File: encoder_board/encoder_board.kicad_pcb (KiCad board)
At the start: 2 copper layers, 40 x 10 mm, 8 parts, among them J1 Conn_01x06, U1 AS5048A

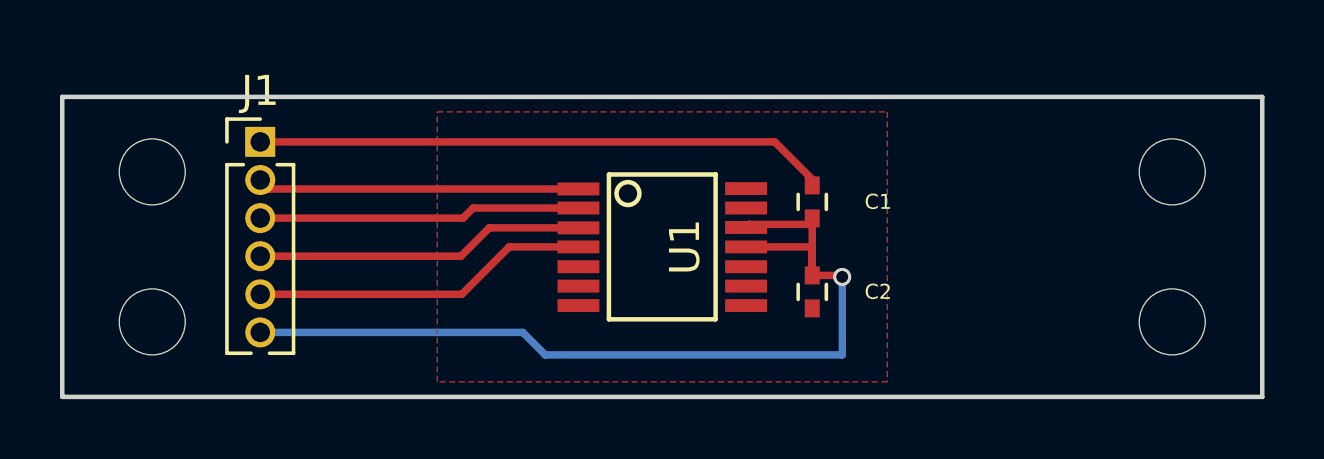
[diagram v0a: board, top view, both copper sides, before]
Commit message: move ground plane to back
 - rexport encoder step
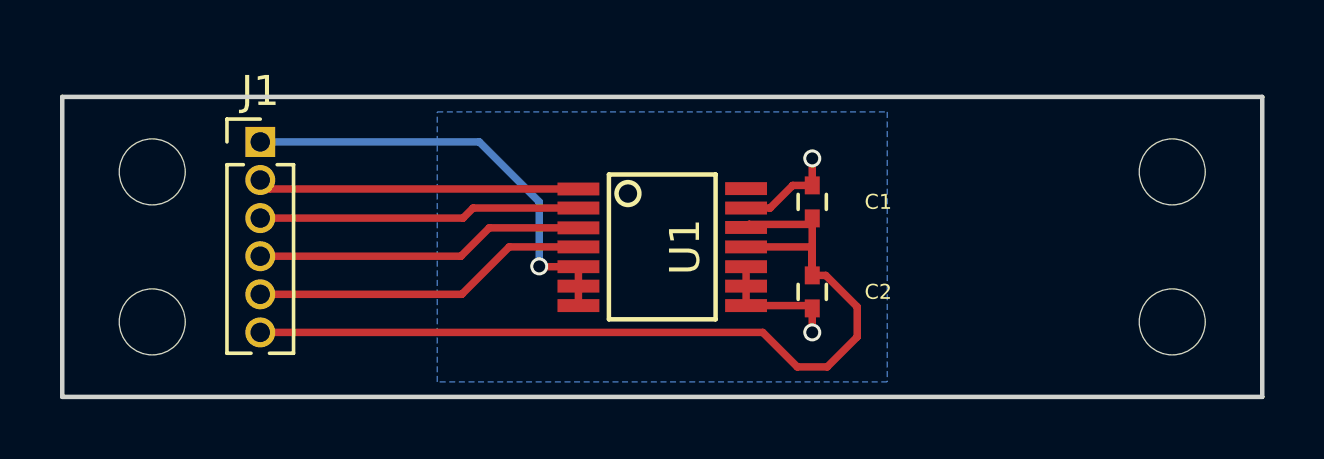
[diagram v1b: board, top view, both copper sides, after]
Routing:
- net GND: track 18.9 -> 22.6 mm, vias 0 -> 3
- net +3V3: track 30.9 -> 31.2 mm, vias 1 -> 0
- added copper zone on B.Cu, net GND
- removed copper zone on F.Cu, net GND
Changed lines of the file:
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@@
     (thickness 1.6)
     (drawings 6)
-    (tracks 27)
+    (tracks 44)
     (zones 0)
     (modules 8)
@@
   (gr_line (start 140 100) (end 140 110) (angle 90) (layer Edge.Cuts) (width 0.15))
   (gr_line (start 100 100) (end 140 100) (angle 90) (layer Edge.Cuts) (width 0.15))
-  (segment (start 106.6 101.5) (end 123.75 101.5) (width 0.25) (layer F.Cu) (net 1) (status 10))
-  (segment (start 123.75 101.5) (end 125 102.75) (width 0.25) (layer F.Cu) (net 1))
-  (segment (start 125 105.95) (end 125.95 105.95) (width 0.25) (layer F.Cu) (net 3))
-  (segment (start 115.35 107.85) (end 106.6 107.85) (width 0.25) (layer B.Cu) (net 3))
-  (segment (start 116.1 108.6) (end 115.35 107.85) (width 0.25) (layer B.Cu) (net 3))
-  (segment (start 126 108.6) (end 116.1 108.6) (width 0.25) (layer B.Cu) (net 3))
-  (segment (start 126 106) (end 126 108.6) (width 0.25) (layer B.Cu) (net 3))
-  (via (at 126 106) (size 0.6) (drill 0.4) (layers F.Cu B.Cu) (net 3))
-  (segment (start 125.95 105.95) (end 126 106) (width 0.25) (layer F.Cu) (net 3))
+  (segment (start 125 107.05) (end 125 107.85) (width 0.25) (layer F.Cu) (net 1) (status 400000))
+  (via (at 125 107.85) (size 0.6) (drill 0.4) (layers F.Cu B.Cu) (net 1))
+  (segment (start 122.794 106.9558) (end 124.9058 106.9558) (width 0.25) (layer F.Cu) (net 1) (status C00000))
+  (segment (start 124.9058 106.9558) (end 125 107.05) (width 0.25) (layer F.Cu) (net 1) (status C00000))
+  (segment (start 125 102.95) (end 125 102.05) (width 0.25) (layer F.Cu) (net 1) (status 400000))
+  (via (at 125 102.05) (size 0.6) (drill 0.4) (layers F.Cu B.Cu) (net 1))
+  (segment (start 122.794 103.7046) (end 123.5954 103.7046) (width 0.25) (layer F.Cu) (net 1) (status 400000))
+  (segment (start 124.35 102.95) (end 125 102.95) (width 0.25) (layer F.Cu) (net 1) (status 800000))
+  (segment (start 123.5954 103.7046) (end 124.35 102.95) (width 0.25) (layer F.Cu) (net 1))
+  (segment (start 122.794 106.3081) (end 122.794 105.6604) (width 0.25) (layer F.Cu) (net 1) (status C00000))
+  (segment (start 122.794 106.9558) (end 122.794 106.3081) (width 0.25) (layer F.Cu) (net 1) (status C00000))
+  (segment (start 117.206 106.3081) (end 117.206 105.6604) (width 0.25) (layer F.Cu) (net 1) (status C00000))
+  (segment (start 117.206 106.9558) (end 117.206 106.3081) (width 0.25) (layer F.Cu) (net 1) (status C00000))
+  (segment (start 106.6 101.5) (end 113.9 101.5) (width 0.25) (layer B.Cu) (net 1) (status 400000))
+  (segment (start 113.9 101.5) (end 115.9 103.5) (width 0.25) (layer B.Cu) (net 1))
+  (segment (start 115.9 103.5) (end 115.9 105.65) (width 0.25) (layer B.Cu) (net 1))
+  (segment (start 115.9104 105.6604) (end 117.206 105.6604) (width 0.25) (layer F.Cu) (net 1) (status 800000))
+  (via (at 115.9 105.65) (size 0.6) (drill 0.4) (layers F.Cu B.Cu) (net 1))
+  (segment (start 115.9104 105.6604) (end 115.9 105.65) (width 0.25) (layer F.Cu) (net 1))
+  (segment (start 106.6 107.85) (end 123.35 107.85) (width 0.25) (layer F.Cu) (net 3) (status 400000))
+  (segment (start 125.45 105.95) (end 125 105.95) (width 0.25) (layer F.Cu) (net 3) (status 800000))
+  (segment (start 126.5 107) (end 125.45 105.95) (width 0.25) (layer F.Cu) (net 3))
+  (segment (start 126.5 108) (end 126.5 107) (width 0.25) (layer F.Cu) (net 3))
+  (segment (start 125.5 109) (end 126.5 108) (width 0.25) (layer F.Cu) (net 3))
+  (segment (start 124.5 109) (end 125.5 109) (width 0.25) (layer F.Cu) (net 3))
+  (segment (start 123.35 107.85) (end 124.5 109) (width 0.25) (layer F.Cu) (net 3))
   (segment (start 125 105.95) (end 125 105) (width 0.25) (layer F.Cu) (net 3))
   (segment (start 125 105) (end 122.794 105) (width 0.25) (layer F.Cu) (net 3))
@@
   (segment (start 113.32 106.58) (end 114.9 105) (width 0.25) (layer F.Cu) (net 7))
   (segment (start 114.9 105) (end 117.206 105) (width 0.25) (layer F.Cu) (net 7))
-  (zone (net 1) (net_name GND) (layer F.Cu) (hatch edge 0.508)
+  (zone (net 1) (net_name GND) (layer B.Cu) (hatch edge 0.508)
     (connect_pads (clearance 0.25))
     (min_thickness 0.25)

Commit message: apply cosine's suggestions about gnd plane
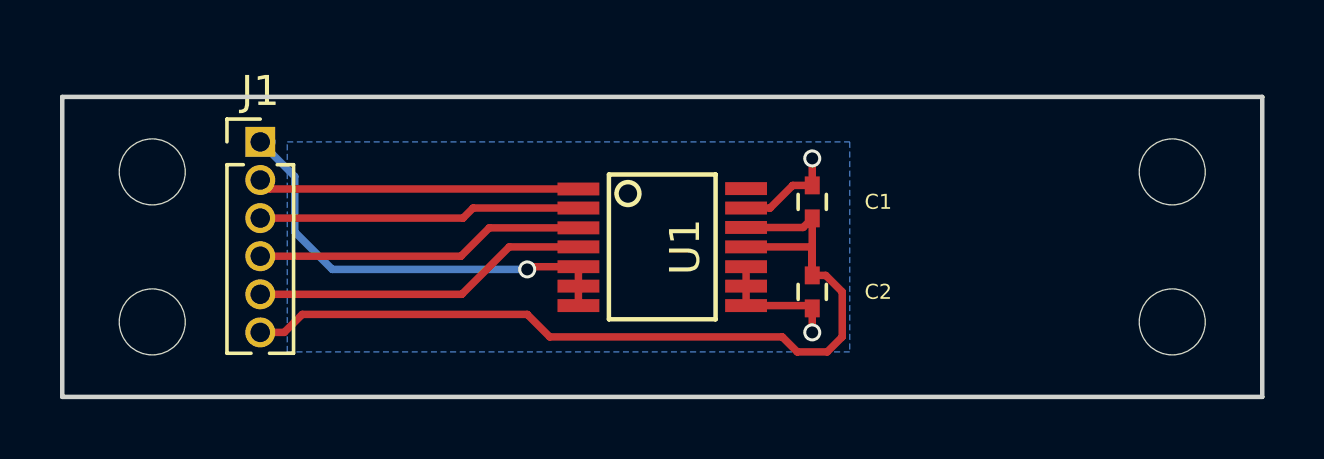
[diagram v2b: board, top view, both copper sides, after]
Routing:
- net +3V3: track 31.2 -> 30.6 mm
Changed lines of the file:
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@@
     (links 17)
     (no_connects 0)
-    (area 99.924999 99.924999 140.075001 110.075001)
+    (area 92.942857 98.325 146.057143 112.575)
     (thickness 1.6)
     (drawings 6)
-    (tracks 44)
+    (tracks 49)
     (zones 0)
     (modules 8)
@@
       (outputformat 1)
       (mirror false)
-      (drillshape 1)
+      (drillshape 0)
       (scaleselection 1)
-      (outputdirectory ""))
+      (outputdirectory /home/peter/Projects/sm/Smartmouse_pcbs_2018/encoder_board/gerber))
   )
   (net 0 "")
@@
   )
   (gr_line (start 100.5 105) (end 139.5 105) (angle 90) (layer Cmts.User) (width 0.2))
-  (gr_line (start 120 99.5) (end 120 109.5) (angle 90) (layer Cmts.User) (width 0.2))
+  (gr_line (start 120 100.5) (end 120 109.5) (angle 90) (layer Cmts.User) (width 0.2))
   (gr_line (start 100 110) (end 100 100) (angle 90) (layer Edge.Cuts) (width 0.15))
   (gr_line (start 140 110) (end 100 110) (angle 90) (layer Edge.Cuts) (width 0.15))
   (gr_line (start 140 100) (end 140 110) (angle 90) (layer Edge.Cuts) (width 0.15))
   (gr_line (start 100 100) (end 140 100) (angle 90) (layer Edge.Cuts) (width 0.15))
-  (segment (start 125 107.05) (end 125 107.85) (width 0.25) (layer F.Cu) (net 1) (status 400000))
+  (segment (start 117.206 105.6604) (end 115.5896 105.6604) (width 0.25) (layer F.Cu) (net 1))
+  (segment (start 107.75 102.65) (end 106.6 101.5) (width 0.25) (layer B.Cu) (net 1))
+  (segment (start 107.75 104.5) (end 107.75 102.65) (width 0.25) (layer B.Cu) (net 1))
+  (segment (start 109 105.75) (end 107.75 104.5) (width 0.25) (layer B.Cu) (net 1))
+  (segment (start 115.5 105.75) (end 109 105.75) (width 0.25) (layer B.Cu) (net 1))
+  (via (at 115.5 105.75) (size 0.6) (drill 0.4) (layers F.Cu B.Cu) (net 1))
+  (segment (start 115.5896 105.6604) (end 115.5 105.75) (width 0.25) (layer F.Cu) (net 1))
+  (segment (start 106.6 101.5) (end 107 101.5) (width 0.25) (layer B.Cu) (net 1))
+  (segment (start 125 107.05) (end 125 107.85) (width 0.25) (layer F.Cu) (net 1))
   (via (at 125 107.85) (size 0.6) (drill 0.4) (layers F.Cu B.Cu) (net 1))
-  (segment (start 122.794 106.9558) (end 124.9058 106.9558) (width 0.25) (layer F.Cu) (net 1) (status C00000))
-  (segment (start 124.9058 106.9558) (end 125 107.05) (width 0.25) (layer F.Cu) (net 1) (status C00000))
-  (segment (start 125 102.95) (end 125 102.05) (width 0.25) (layer F.Cu) (net 1) (status 400000))
+  (segment (start 122.794 106.9558) (end 124.9058 106.9558) (width 0.25) (layer F.Cu) (net 1))
+  (segment (start 124.9058 106.9558) (end 125 107.05) (width 0.25) (layer F.Cu) (net 1))
+  (segment (start 125 102.95) (end 125 102.05) (width 0.25) (layer F.Cu) (net 1))
   (via (at 125 102.05) (size 0.6) (drill 0.4) (layers F.Cu B.Cu) (net 1))
-  (segment (start 122.794 103.7046) (end 123.5954 103.7046) (width 0.25) (layer F.Cu) (net 1) (status 400000))
-  (segment (start 124.35 102.95) (end 125 102.95) (width 0.25) (layer F.Cu) (net 1) (status 800000))
+  (segment (start 122.794 103.7046) (end 123.5954 103.7046) (width 0.25) (layer F.Cu) (net 1))
+  (segment (start 124.35 102.95) (end 125 102.95) (width 0.25) (layer F.Cu) (net 1))
   (segment (start 123.5954 103.7046) (end 124.35 102.95) (width 0.25) (layer F.Cu) (net 1))
-  (segment (start 122.794 106.3081) (end 122.794 105.6604) (width 0.25) (layer F.Cu) (net 1) (status C00000))
-  (segment (start 122.794 106.9558) (end 122.794 106.3081) (width 0.25) (layer F.Cu) (net 1) (status C00000))
-  (segment (start 117.206 106.3081) (end 117.206 105.6604) (width 0.25) (layer F.Cu) (net 1) (status C00000))
-  (segment (start 117.206 106.9558) (end 117.206 106.3081) (width 0.25) (layer F.Cu) (net 1) (status C00000))
-  (segment (start 106.6 101.5) (end 113.9 101.5) (width 0.25) (layer B.Cu) (net 1) (status 400000))
-  (segment (start 113.9 101.5) (end 115.9 103.5) (width 0.25) (layer B.Cu) (net 1))
-  (segment (start 115.9 103.5) (end 115.9 105.65) (width 0.25) (layer B.Cu) (net 1))
-  (segment (start 115.9104 105.6604) (end 117.206 105.6604) (width 0.25) (layer F.Cu) (net 1) (status 800000))
-  (via (at 115.9 105.65) (size 0.6) (drill 0.4) (layers F.Cu B.Cu) (net 1))
-  (segment (start 115.9104 105.6604) (end 115.9 105.65) (width 0.25) (layer F.Cu) (net 1))
-  (segment (start 106.6 107.85) (end 123.35 107.85) (width 0.25) (layer F.Cu) (net 3) (status 400000))
-  (segment (start 125.45 105.95) (end 125 105.95) (width 0.25) (layer F.Cu) (net 3) (status 800000))
-  (segment (start 126.5 107) (end 125.45 105.95) (width 0.25) (layer F.Cu) (net 3))
-  (segment (start 126.5 108) (end 126.5 107) (width 0.25) (layer F.Cu) (net 3))
-  (segment (start 125.5 109) (end 126.5 108) (width 0.25) (layer F.Cu) (net 3))
-  (segment (start 124.5 109) (end 125.5 109) (width 0.25) (layer F.Cu) (net 3))
-  (segment (start 123.35 107.85) (end 124.5 109) (width 0.25) (layer F.Cu) (net 3))
+  (segment (start 122.794 106.3081) (end 122.794 105.6604) (width 0.25) (layer F.Cu) (net 1))
+  (segment (start 122.794 106.9558) (end 122.794 106.3081) (width 0.25) (layer F.Cu) (net 1))
+  (segment (start 117.206 106.3081) (end 117.206 105.6604) (width 0.25) (layer F.Cu) (net 1))
+  (segment (start 117.206 106.9558) (end 117.206 106.3081) (width 0.25) (layer F.Cu) (net 1))
+  (segment (start 122.794 104.3523) (end 124.6977 104.3523) (width 0.25) (layer F.Cu) (net 3))
+  (segment (start 124.6977 104.3523) (end 125 104.05) (width 0.25) (layer F.Cu) (net 3))
+  (segment (start 106.6 107.85) (end 107.4 107.85) (width 0.25) (layer F.Cu) (net 3))
+  (segment (start 125.45 105.95) (end 125 105.95) (width 0.25) (layer F.Cu) (net 3))
+  (segment (start 126 106.5) (end 125.45 105.95) (width 0.25) (layer F.Cu) (net 3))
+  (segment (start 126 108) (end 126 106.5) (width 0.25) (layer F.Cu) (net 3))
+  (segment (start 125.5 108.5) (end 126 108) (width 0.25) (layer F.Cu) (net 3))
+  (segment (start 124.5 108.5) (end 125.5 108.5) (width 0.25) (layer F.Cu) (net 3))
+  (segment (start 124 108) (end 124.5 108.5) (width 0.25) (layer F.Cu) (net 3))
+  (segment (start 116.25 108) (end 124 108) (width 0.25) (layer F.Cu) (net 3))
+  (segment (start 115.5 107.25) (end 116.25 108) (width 0.25) (layer F.Cu) (net 3))
+  (segment (start 108 107.25) (end 115.5 107.25) (width 0.25) (layer F.Cu) (net 3))
+  (segment (start 107.4 107.85) (end 108 107.25) (width 0.25) (layer F.Cu) (net 3))
   (segment (start 125 105.95) (end 125 105) (width 0.25) (layer F.Cu) (net 3))
   (segment (start 125 105) (end 122.794 105) (width 0.25) (layer F.Cu) (net 3))
   (segment (start 106.65 107.9) (end 106.6 107.85) (width 0.25) (layer F.Cu) (net 3))
   (segment (start 125 105.95) (end 125 104.05) (width 0.25) (layer F.Cu) (net 3))
-  (segment (start 125 104.25) (end 122.8963 104.25) (width 0.25) (layer F.Cu) (net 3))
-  (segment (start 122.8963 104.25) (end 122.794 104.3523) (width 0.25) (layer F.Cu) (net 3))
-  (segment (start 122.8963 104.25) (end 122.794 104.3523) (width 0.25) (layer F.Cu) (net 3))
   (segment (start 117.206 103.0696) (end 106.8996 103.0696) (width 0.25) (layer F.Cu) (net 4) (status 20))
   (segment (start 106.8996 103.0696) (end 106.6 102.77) (width 0.25) (layer F.Cu) (net 4) (status 30))
@@
     (polygon
       (pts
-        (xy 127.5 109.5) (xy 112.5 109.5) (xy 112.5 100.5) (xy 127.5 100.5)
+        (xy 126.25 108.5) (xy 107.5 108.5) (xy 107.5 101.5) (xy 126.25 101.5)
       )
     )
